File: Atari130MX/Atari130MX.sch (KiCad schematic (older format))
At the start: 89 parts, among them J1 Conn_01x32, J2 Conn_01x26, J3 Conn_01x14, SW1 SW_Push_45deg, SW10 SW_Push_45deg, SW2 SW_Push_45deg, SW3 SW_Push_45deg, SW4 SW_Push_45deg, SW5 SW_Push_45deg, SW6 SW_Push_45deg, SW7 SW_Push_45deg, SW8 SW_Push_45deg, SW9 SW_Push_45deg, U1 PICO_RP2040

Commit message: BUG for LALT & RALT when used in Atari mode. Wrong ROW8 it must be ROW7 Tracks size increased, expecially for GND/POWER signals Added 9U spacebar and stabilizers like Atari keycaps. This is PCB only. The Plate is not compatible with it, at the moment...
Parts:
- added SW1: SPC 9U, RetroBit:SW_Cherry_MX1A_9u_PCB_3d, symbol Switch:SW_Push_45deg
- SW10: renamed from SWSpc2; value SW_Push_45deg -> Right-Alt
- SW11: renamed from SWJ1; value SW_Push_45deg -> J
- SW12: renamed from SWH1; value SW_Push_45deg -> H
- SW13: renamed from SWSpc3; value SW_Push_45deg -> SPC
- SW14: renamed from SWHlp1; value SW_Push_45deg -> Help
- SW15: renamed from SW3; value SW_Push_45deg -> 8
- SW16: renamed from SW4; value SW_Push_45deg -> 5
- SW17: renamed from SWI1; value SW_Push_45deg -> I
- SW18: renamed from SWT1; value SW_Push_45deg -> T
- SW19: renamed from SWK1; value SW_Push_45deg -> K
- SW2: renamed from SWSpc1; value SW_Push_45deg -> Left-Alt
- SW20: renamed from SWG1; value SW_Push_45deg -> G
- SW21: renamed from SWM1; value SW_Push_45deg -> M
- SW22: renamed from SWB1; value SW_Push_45deg -> B
- SW23: renamed from SW5; value SW_Push_45deg -> 9
- SW24: renamed from SW6; value SW_Push_45deg -> 4
- SW25: renamed from SWO1; value SW_Push_45deg -> O
- SW26: renamed from SWR1; value SW_Push_45deg -> R
- SW27: renamed from SWL1; value SW_Push_45deg -> L
- SW28: renamed from SWF1; value SW_Push_45deg -> F
- SW29: renamed from SWComma1; value SW_Push_45deg -> ,
- SW3: renamed from SW1; value SW_Push_45deg -> 7
- SW30: renamed from SWV1; value SW_Push_45deg -> V
- SW31: renamed from SW7; value SW_Push_45deg -> 0
- SW32: renamed from SW8; value SW_Push_45deg -> 3
- SW33: renamed from SWP1; value SW_Push_45deg -> P
- SW34: renamed from SWE1; value SW_Push_45deg -> E
- SW35: renamed from SWSemi1; value SW_Push_45deg -> ;
- SW36: renamed from SWD1; value SW_Push_45deg -> D
- SW37: renamed from SWPeriod1; value SW_Push_45deg -> .
- SW38: renamed from SWC1; value SW_Push_45deg -> C
- SW39: renamed from SWLT1; value SW_Push_45deg -> <
- SW4: renamed from SW2; value SW_Push_45deg -> 6
- SW40: renamed from SW9; value SW_Push_45deg -> 2
- SW41: renamed from SWDash1; value SW_Push_45deg -> -
- SW42: renamed from SWW1; value SW_Push_45deg -> W
- SW43: renamed from SWPlus1; value SW_Push_45deg -> +
- SW44: renamed from SWS1; value SW_Push_45deg -> S
- SW45: renamed from SWSlash1; value SW_Push_45deg -> /
- SW46: renamed from SWX1; value SW_Push_45deg -> X
- SW47: renamed from SWGT1; value SW_Push_45deg -> >
- SW48: renamed from SW10; value SW_Push_45deg -> 1
- SW49: renamed from SWEqual1; value SW_Push_45deg -> =
- SW5: renamed from SWU1; value SW_Push_45deg -> U
- SW50: renamed from SWQ1; value SW_Push_45deg -> Q
- SW51: renamed from SWStar1; value SW_Push_45deg -> *
- SW52: renamed from SWA1; value SW_Push_45deg -> A
- SW53: renamed from SWInv1; value SW_Push_45deg -> FUJI
- SW54: renamed from SWZ1; value SW_Push_45deg -> Z
- SW55: renamed from SWDel1; value SW_Push_45deg -> Del
- SW56: renamed from SWEsc1; value SW_Push_45deg -> Esc
- SW57: renamed from SWRet1; value SW_Push_45deg -> Return
- SW58: renamed from SWTab1; value SW_Push_45deg -> Tab
- SW59: renamed from SWFn3; value SW_Push_45deg -> F2
- SW6: renamed from SWY1; value SW_Push_45deg -> Y
- SW60: renamed from SWCps1; value SW_Push_45deg -> Caps
- SW61: renamed from SWFn4; value SW_Push_45deg -> F4
- SW62: renamed from SWBrk1; value SW_Push_45deg -> Break
- SW63: renamed from SWCtl1; value SW_Push_45deg -> Ctrl
- SW64: renamed from SWRightSft1; value SW_Push_45deg -> RSC
- SW65: renamed from SWLeftSft1; value SW_Push_45deg -> LSC
- SW66: renamed from SWStart1; value SW_Push_45deg -> Start
- SW67: renamed from SWSelect1; value SW_Push_45deg -> Select
- SW68: renamed from SWOption1; value SW_Push_45deg -> Option
- SW69: renamed from SWReset1; value SW_Push_45deg -> Reset
- SW7: renamed from SWFn1; value SW_Push_45deg -> F1
- SW8: renamed from SWN1; value SW_Push_45deg -> N
- SW9: renamed from SWFn2; value SW_Push_45deg -> F3
- renumbered L2 to L1, L3 to L2, L4 to L3, L5 to L4, L6 to L5, L7 to L6, L1 to L7
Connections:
- net COL_2: now also SW1.1
- net ROW_7: now also JP1.3 (B), JP2.3 (B), SW1.2
- net ROW_8: no longer JP1.3 (B), JP2.3 (B)
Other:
- note added: "ATARI MODE 2-3\nLALT MODE 1-2\nRALT MODE 1-2"
- note added: "ATARI MODE 2-3\nUSB LEFT SHIFT 1-2"
- note added: "SPACEBAR 9U"
- note removed: "ATARI 2-3\nLALT 1-2\nRALT 1-2"
- note removed: "ATARI 2-3\nUSB LEFT SHIFT 1-2"

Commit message: Added extra holes for 6.25U, 9U and stabilizers holes. Added extra holes for mounting on top cover if exist.
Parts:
- added H5, H6, H7, H8: MountingHole, MountingHole:MountingHole_3.2mm_M3, symbol Mechanical:MountingHole
- SW10: footprint Atari130MX:SW_Kailh_1.50u_PCB -> Atari130MX:SW_Kailh_1.25u_PCB
- SW2: footprint Atari130MX:SW_Kailh_1.25u_PCB -> Atari130MX:SW_Kailh_1.50u_PCB
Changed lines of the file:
@@
 Sheet 1 1
 Title "Atari XE Mechanical Keyboard"
-Date "2021-12-30"
+Date "2021-12-31"
 Rev "E"
 Comp "Decent Consulting"
@@
 F 0 "SW2" H 2700 7350 50  0000 C CNN
 F 1 "Left-Alt" H 2500 7600 50  0000 C CNN
-F 2 "Atari130MX:SW_Kailh_1.25u_PCB" H 2800 7400 50  0001 C CNN
+F 2 "Atari130MX:SW_Kailh_1.50u_PCB" H 2800 7400 50  0001 C CNN
 F 3 "~" H 2800 7400 50  0001 C CNN
 	1    2800 7400
@@
 F 0 "SW10" H 3450 7350 50  0000 C CNN
 F 1 "Right-Alt" H 3650 7650 50  0000 C CNN
-F 2 "Atari130MX:SW_Kailh_1.50u_PCB" H 3550 7400 50  0001 C CNN
+F 2 "Atari130MX:SW_Kailh_1.25u_PCB" H 3550 7400 50  0001 C CNN
 F 3 "~" H 3550 7400 50  0001 C CNN
 	1    3550 7400
@@
 Wire Wire Line
 	12200 7750 12200 7900
+$Comp
+L Mechanical:MountingHole H5
+U 1 1 61CFBB35
+P 10700 9050
+F 0 "H5" H 10800 9100 50  0000 L CNN
+F 1 "MountingHole" H 10800 9050 50  0000 L CNN
+F 2 "MountingHole:MountingHole_3.2mm_M3" H 10700 9050 50  0001 C CNN
+F 3 "~" H 10700 9050 50  0001 C CNN
+	1    10700 9050
+	1    0    0    -1
+$EndComp
+$Comp
+L Mechanical:MountingHole H6
+U 1 1 61CFBCB7
+P 11400 9050
+F 0 "H6" H 11500 9100 50  0000 L CNN
+F 1 "MountingHole" H 11500 9050 50  0000 L CNN
+F 2 "MountingHole:MountingHole_3.2mm_M3" H 11400 9050 50  0001 C CNN
+F 3 "~" H 11400 9050 50  0001 C CNN
+	1    11400 9050
+	1    0    0    -1
+$EndComp
+$Comp
+L Mechanical:MountingHole H7
+U 1 1 61CFBE8D
+P 12100 9050
+F 0 "H7" H 12200 9100 50  0000 L CNN
+F 1 "MountingHole" H 12200 9050 50  0000 L CNN
+F 2 "MountingHole:MountingHole_3.2mm_M3" H 12100 9050 50  0001 C CNN
+F 3 "~" H 12100 9050 50  0001 C CNN
+	1    12100 9050
+	1    0    0    -1
+$EndComp
+$Comp
+L Mechanical:MountingHole H8
+U 1 1 61CFC049
+P 12800 9050
+F 0 "H8" H 12900 9100 50  0000 L CNN
+F 1 "MountingHole" H 12900 9050 50  0000 L CNN
+F 2 "MountingHole:MountingHole_3.2mm_M3" H 12800 9050 50  0001 C CNN
+F 3 "~" H 12800 9050 50  0001 C CNN
+	1    12800 9050
+	1    0    0    -1
+$EndComp
 $EndSCHEMATC

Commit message: Using Atari spacebar (not fully 9U lenght). Other keys layout must be adapted a little bit.
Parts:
- SW1: footprint RetroBit:SW_Cherry_MX1A_9u_PCB_3d -> Atari130MX:SW_Kailh_Atari_Space
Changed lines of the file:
@@
 F 0 "SW1" H 2000 6631 50  0000 C CNN
 F 1 "SPC 9U" H 2000 6540 50  0000 C CNN
-F 2 "RetroBit:SW_Cherry_MX1A_9u_PCB_3d" H 2000 6350 50  0001 C CNN
+F 2 "Atari130MX:SW_Kailh_Atari_Space" H 2000 6350 50  0001 C CNN
 F 3 "~" H 2000 6350 50  0001 C CNN
 	1    2000 6350

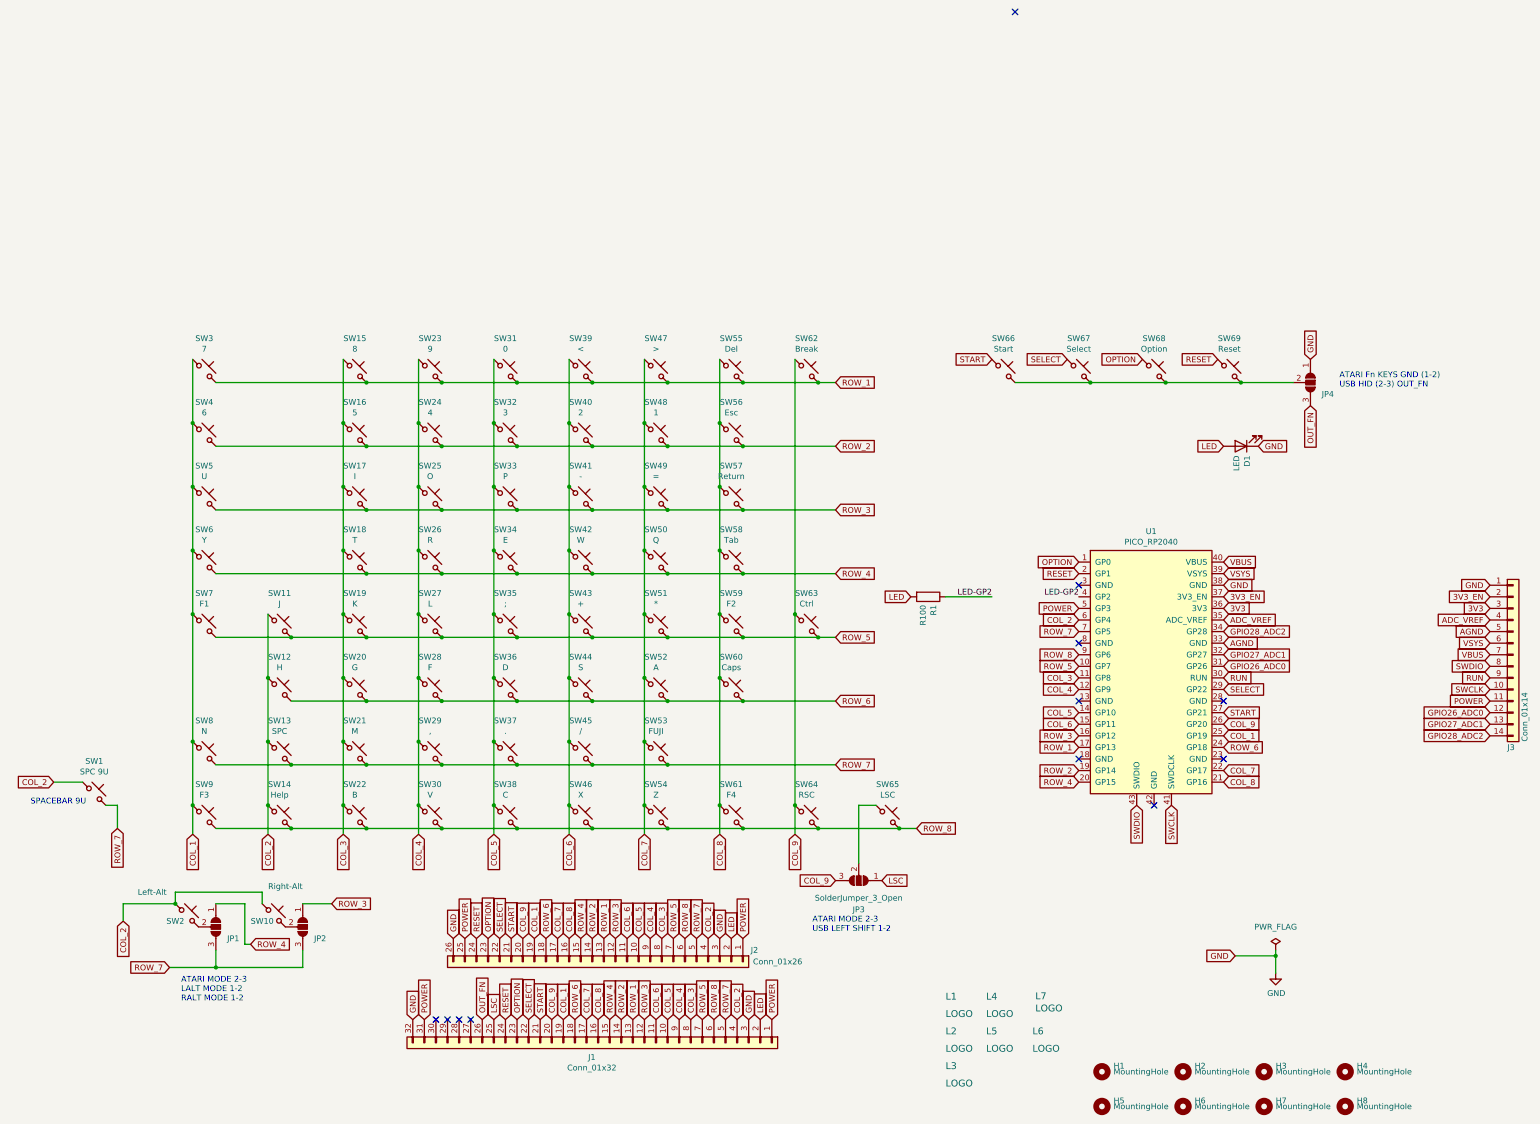
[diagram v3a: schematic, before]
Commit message: It's simpler to use a (almost) standard 7U spacebar and two 1u extra keys. In that way, the holes needed are only for extra 9U stabilizers. Even the plate gets simpler.
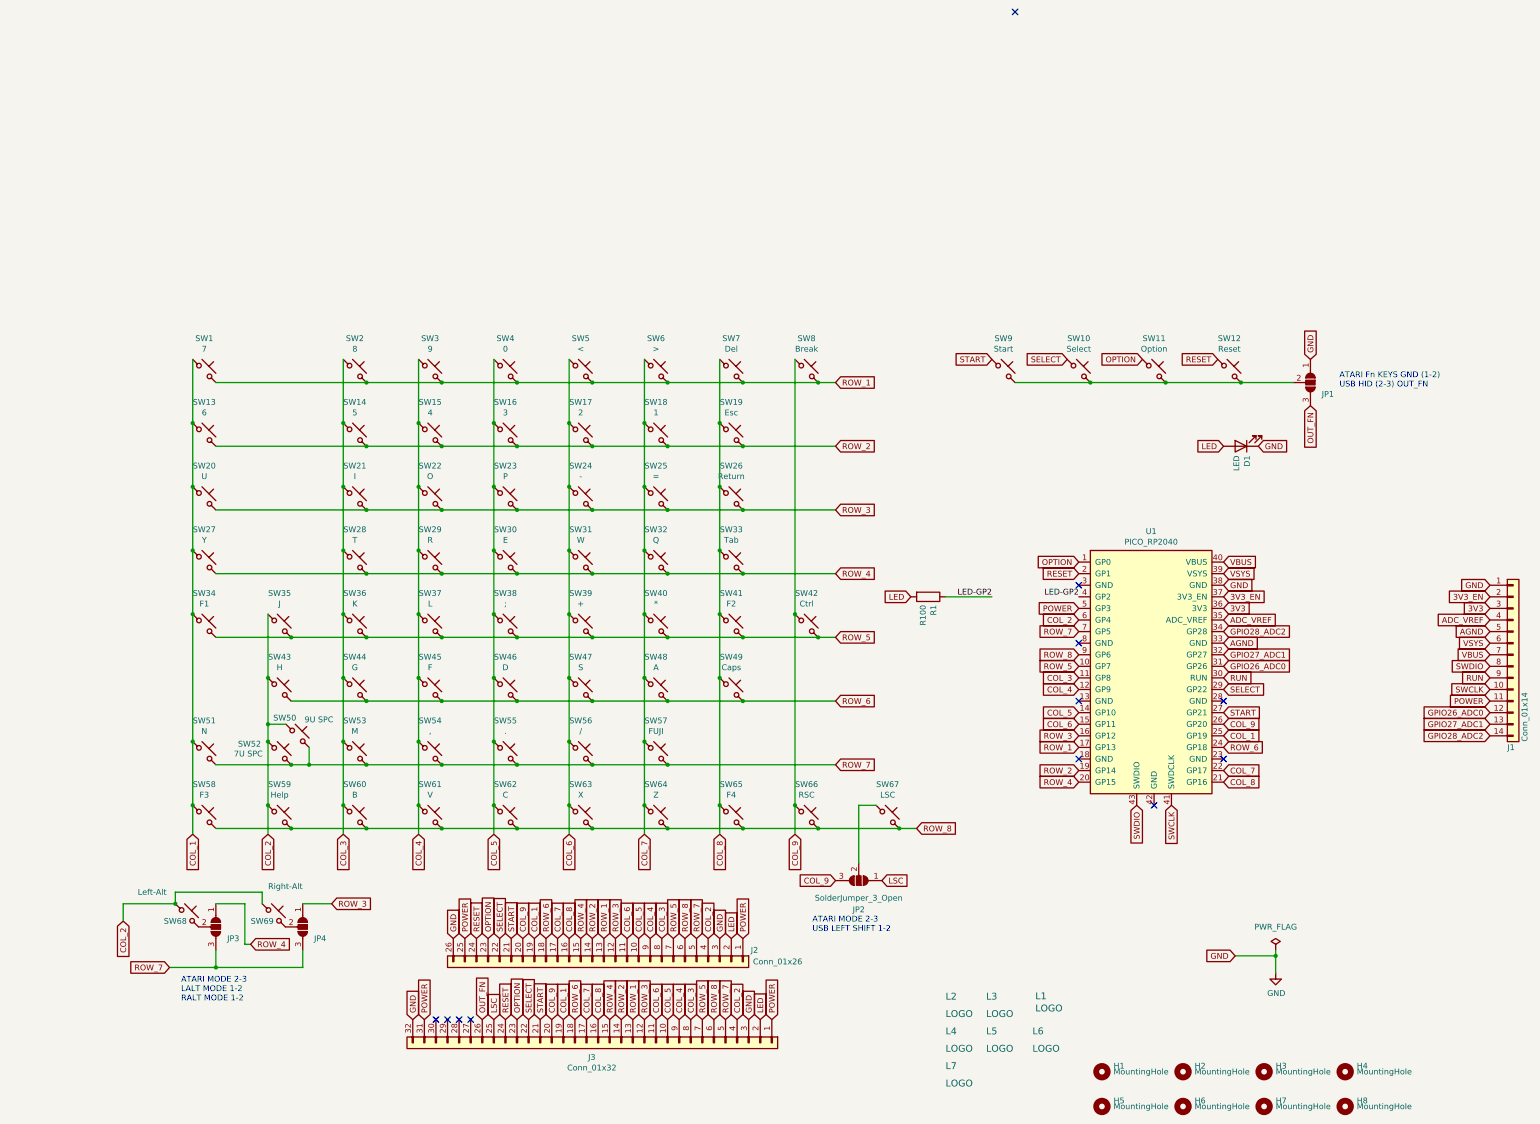
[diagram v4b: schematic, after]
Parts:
- removed SW1: SPC 9U, Atari130MX:SW_Kailh_Atari_Space, symbol Switch:SW_Push_45deg
- added SW50: 9U SPC, RetroBit:SW_Cherry_MX1A_9u_PCB_noSwitch, symbol Switch:SW_Push_45deg
- SW52: renamed from SW13; value SPC -> 7U SPC; footprint RetroBit:SW_Cherry_MX1A_6.25u_PCB_3d -> RetroBit:MXOnly-7U-NoLED
- SW68: renamed from SW2; footprint Atari130MX:SW_Kailh_1.50u_PCB -> Atari130MX:SW_Kailh_1.00u_PCB
- SW69: renamed from SW10; footprint Atari130MX:SW_Kailh_1.25u_PCB -> Atari130MX:SW_Kailh_1.00u_PCB
- renumbered J3 to J1, J1 to J3, JP4 to JP1, JP3 to JP2, JP1 to JP3, JP2 to JP4, L7 to L1, L1 to L2, L4 to L3, L2 to L4, L3 to L7, SW3 to SW1, SW67 to SW10, SW68 to SW11, SW69 to SW12, SW4 to SW13, SW16 to SW14, SW24 to SW15, SW32 to SW16, SW40 to SW17, SW48 to SW18, SW56 to SW19, SW15 to SW2, SW5 to SW20, SW17 to SW21, SW25 to SW22, SW33 to SW23, SW41 to SW24, SW49 to SW25, SW57 to SW26, SW6 to SW27, SW18 to SW28, SW26 to SW29, SW23 to SW3, SW34 to SW30, SW42 to SW31, SW50 to SW32, SW58 to SW33, SW7 to SW34, SW11 to SW35, SW19 to SW36, SW27 to SW37, SW35 to SW38, SW43 to SW39, SW31 to SW4, SW51 to SW40, SW59 to SW41, SW63 to SW42, SW12 to SW43, SW20 to SW44, SW28 to SW45, SW36 to SW46, SW44 to SW47, SW52 to SW48, SW60 to SW49, SW39 to SW5, SW8 to SW51, SW21 to SW53, SW29 to SW54, SW37 to SW55, SW45 to SW56, SW53 to SW57, SW9 to SW58, SW14 to SW59, SW47 to SW6, SW22 to SW60, SW30 to SW61, SW38 to SW62, SW46 to SW63, SW54 to SW64, SW61 to SW65, SW64 to SW66, SW65 to SW67, SW55 to SW7, SW62 to SW8, SW66 to SW9
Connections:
- net COL_2: now also SW50.1
- net ROW_7: now also SW50.2
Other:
- note removed: "SPACEBAR 9U"

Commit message: Removed the original FFC connector. This will lose any compatibility between two projects
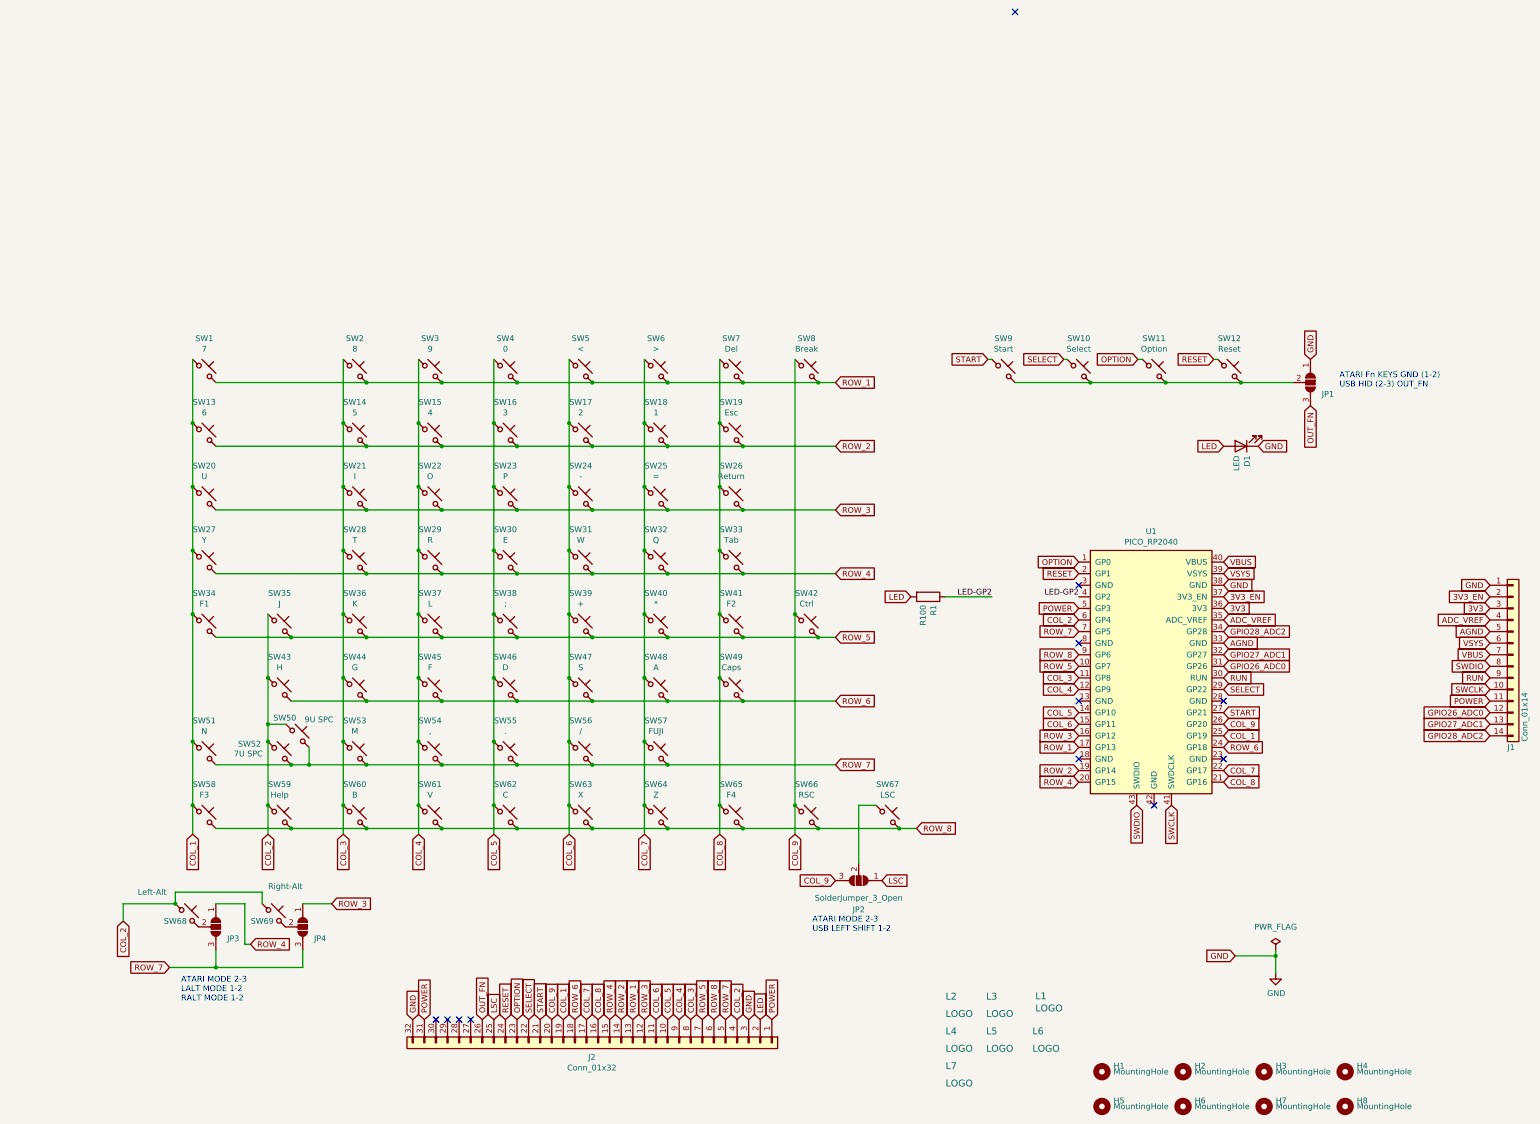
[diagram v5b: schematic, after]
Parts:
- removed J2: Conn_01x26, Atari130MX:Molex_200528-0260_1x26-1MP_P1.00mm_Horizontal, symbol Connector_Generic:Conn_01x26
- renumbered J3 to J2
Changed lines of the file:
@@
 Sheet 1 1
 Title "Atari XE Mechanical Keyboard"
-Date "2022-01-12"
-Rev "D"
+Date "2022-01-21"
+Rev "Jan 2022"
 Comp "Decent Consulting"
 Comment1 "RetroBitLab Modifications"
-Comment2 ""
+Comment2 "Removed old FFC connector"
 Comment3 ""
 Comment4 ""
@@
 	1    14250 5150
 	1    0    0    -1
-$EndComp
-$Comp
-L Connector_Generic:Conn_01x26 J2
-U 1 1 6147FD17
-P 6400 7800
-F 0 "J2" V 6300 9100 50  0000 C CNN
-F 1 "Conn_01x26" V 6400 9300 50  0000 C CNN
-F 2 "Atari130MX:Molex_200528-0260_1x26-1MP_P1.00mm_Horizontal" H 6400 7800 50  0001 C CNN
-F 3 "~" H 6400 7800 50  0001 C CNN
-	1    6400 7800
-	0    1    1    0
 $EndComp
 Wire Wire Line
@@
 Text GLabel 8050 6700 3    50   Input ~ 0
 COL_9
-Text GLabel 9750 2600 0    50   Input ~ 0
+Text GLabel 9715 2600 0    50   Input ~ 0
 START
-Text GLabel 10400 2600 0    50   Input ~ 0
+Text GLabel 10370 2600 0    50   Input ~ 0
 SELECT
-Text GLabel 11050 2600 0    50   Input ~ 0
+Text GLabel 11010 2600 0    50   Input ~ 0
 OPTION
 Wire Wire Line
@@
 Wire Wire Line
 	2850 2600 2850 3150
-Text GLabel 5800 7600 1    50   Input ~ 0
-COL_1
 Wire Wire Line
 	2850 6450 2850 6700
 Connection ~ 2850 6450
-Text GLabel 7300 7600 1    50   Input ~ 0
-COL_2
 Wire Wire Line
 	3500 6700 3500 6450
 Connection ~ 3500 6450
-Text GLabel 6900 7600 1    50   Input ~ 0
-COL_3
 Wire Wire Line
 	4150 3700 4150 4250
-Text GLabel 6800 7600 1    50   Input ~ 0
-COL_4
 Wire Wire Line
 	4800 6450 4800 6700
 Connection ~ 4800 6450
-Text GLabel 11700 2600 0    50   Input ~ 0
+Text GLabel 11665 2600 0    50   Input ~ 0
 RESET
-Text GLabel 6700 7600 1    50   Input ~ 0
-COL_5
-Text GLabel 6600 7600 1    50   Input ~ 0
-COL_6
 Wire Wire Line
 	6100 6450 6100 6700
 Connection ~ 6100 6450
-Text GLabel 6000 7600 1    50   Input ~ 0
-COL_7
 Wire Wire Line
 	6750 6450 6750 6700
 Connection ~ 6750 6450
-Text GLabel 6100 7600 1    50   Input ~ 0
-COL_8
 Wire Wire Line
 	7400 6450 7400 6700
 Connection ~ 7400 6450
-Text GLabel 5700 7600 1    50   Input ~ 0
-COL_9
 Wire Wire Line
 	8050 6450 8050 6700
-Text GLabel 5600 7600 1    50   Input ~ 0
-START
-Text GLabel 5500 7600 1    50   Input ~ 0
-SELECT
-Text GLabel 5400 7600 1    50   Input ~ 0
-OPTION
-Text GLabel 5300 7600 1    50   Input ~ 0
-RESET
-Text GLabel 7500 7600 1    50   Input ~ 0
-LED
-Text GLabel 7600 7600 1    50   Input ~ 0
-POWER
 Text GLabel 14050 5550 0    50   Input ~ 0
 POWER
@@
 Text GLabel 11850 7750 0    50   Input ~ 0
 GND
-Text GLabel 5100 7600 1    50   Input ~ 0
-GND
-Text GLabel 7400 7600 1    50   Input ~ 0
-GND
-Text GLabel 5200 7600 1    50   Input ~ 0
-POWER
-Text GLabel 6300 7600 1    50   Input ~ 0
-ROW_2
-Text GLabel 6500 7600 1    50   Input ~ 0
-ROW_3
-Text GLabel 6200 7600 1    50   Input ~ 0
-ROW_4
 Wire Wire Line
 	4350 4450 5000 4450
-Text GLabel 7000 7600 1    50   Input ~ 0
-ROW_5
 Wire Wire Line
 	3700 5000 4350 5000
-Text GLabel 5900 7600 1    50   Input ~ 0
-ROW_6
-Text GLabel 7200 7600 1    50   Input ~ 0
-ROW_7
 Wire Wire Line
 	3700 6100 3855 6100
-Text GLabel 7100 7600 1    50   Input ~ 0
-ROW_8
 Wire Wire Line
 	5000 2800 5650 2800
-Text GLabel 6400 7600 1    50   Input ~ 0
-ROW_1
 Text GLabel 14050 5150 0    50   Input ~ 0
 VBUS
@@
 SWDIO
 $Comp
-L Connector_Generic:Conn_01x32 J3
+L Connector_Generic:Conn_01x32 J2
 U 1 1 61C502D9
 P 6350 8500
-F 0 "J3" V 6475 8446 50  0000 C CNN
+F 0 "J2" V 6475 8446 50  0000 C CNN
 F 1 "Conn_01x32" V 6566 8446 50  0000 C CNN
 F 2 "RetroBit:MOLEX-FFC-1.25mm-RA-52044-3245" H 6350 8500 50  0001 C CNN
@@
 Wire Wire Line
 	3500 5750 3500 5350
+Wire Wire Line
+	9715 2600 9750 2600
+Wire Wire Line
+	10370 2600 10400 2600
+Wire Wire Line
+	11010 2600 11050 2600
+Wire Wire Line
+	11665 2600 11700 2600
 $EndSCHEMATC
